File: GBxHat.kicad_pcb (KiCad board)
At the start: 2 copper layers, 65 x 30 mm, 30 parts, among them IC1 ATMEGA8515L-8AU, J0 Raspberry Pi, J1 AVR_SPI_6, U3 RT9013, U4 NLAS4157, U5 74LVC1G126SOT353-1, U6 74LVC1G126SOT353-1, X1 8MHz

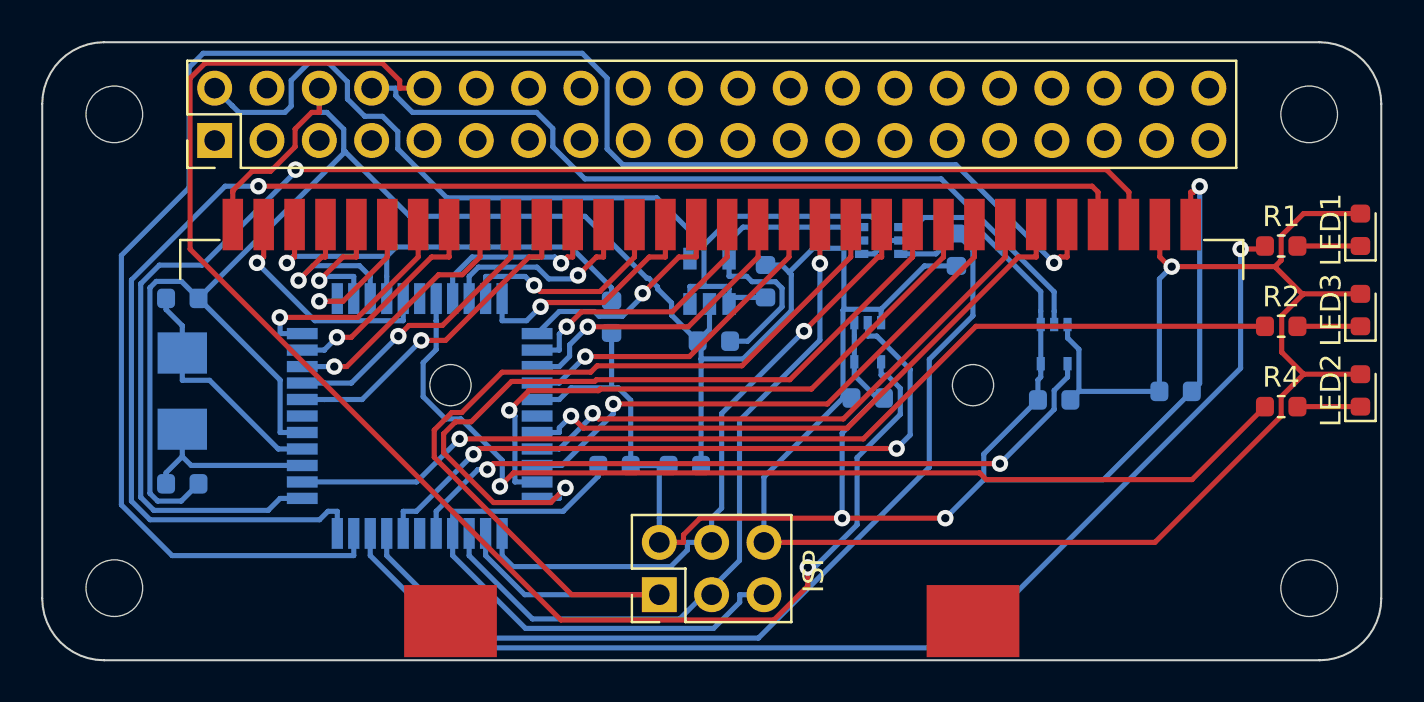
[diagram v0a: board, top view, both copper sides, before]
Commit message: Relocated & Updated LED's
Changed the identifiers for the LED's to match the GBxCart RW

Centered LED's on board
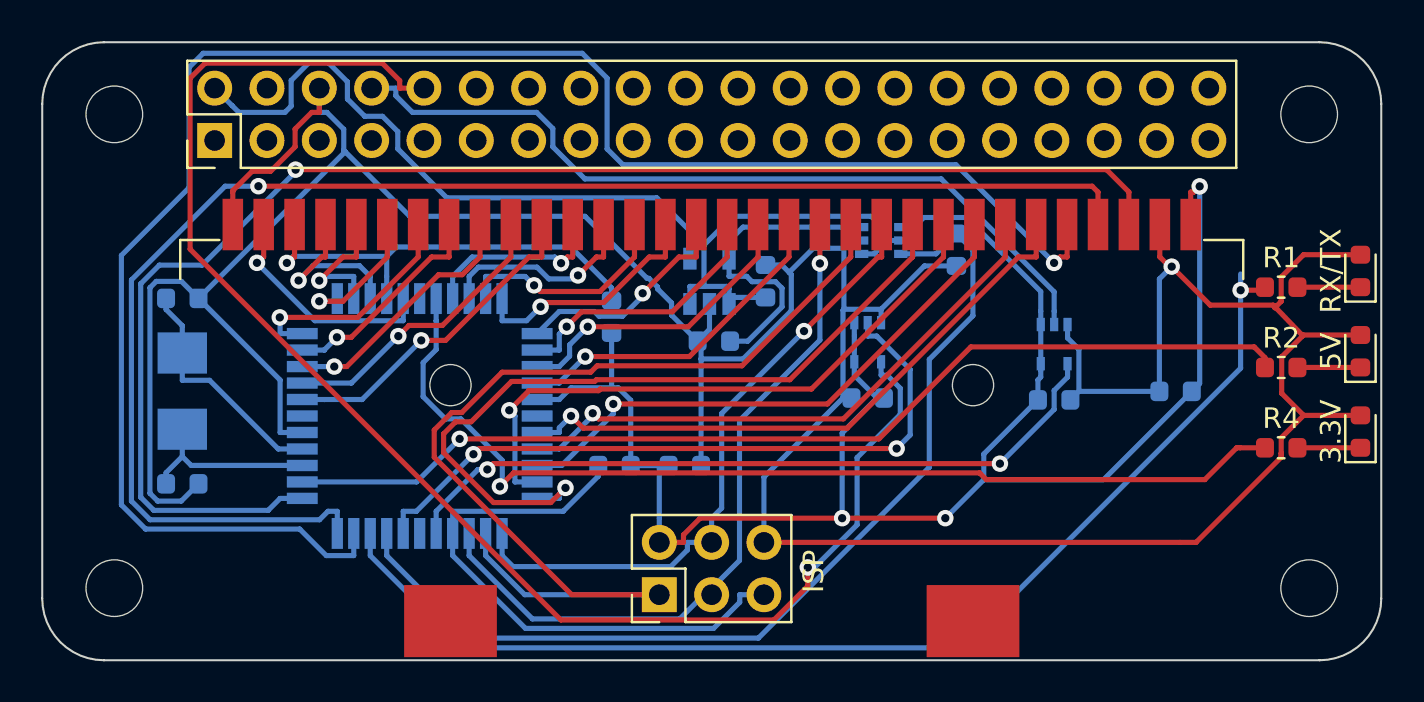
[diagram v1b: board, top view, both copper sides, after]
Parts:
- moved 3.3V 2.00 mm to (264.3, 86.2)
- moved 5V 2.00 mm to (264.3, 82.3)
- moved R1 2.00 mm to (260.4, 79.1)
- moved R2 2.00 mm to (260.4, 83.0)
- moved R4 2.00 mm to (260.4, 86.9)
- moved RX/TX 2.00 mm to (264.3, 78.4)
- renumbered LED2 to 3.3V, LED3 to 5V, LED1 to RX/TX
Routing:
- net Net-(IC1-Pad9): track 57.8 -> 56.6 mm
- net Net-(IC1-Pad29): track 50.5 -> 49.6 mm

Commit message: Fixed logic level issues & removed voltage regulator
- Fixed the issue where 5v logic was connected to the Pi zero which is not 5v tolerant
- Removed the NLAS4157, the 3.3v on the Pi zero itself is now being used instead
- Removed the 74LVC1G126 chips since RX and TX are now connected to the TXB0108
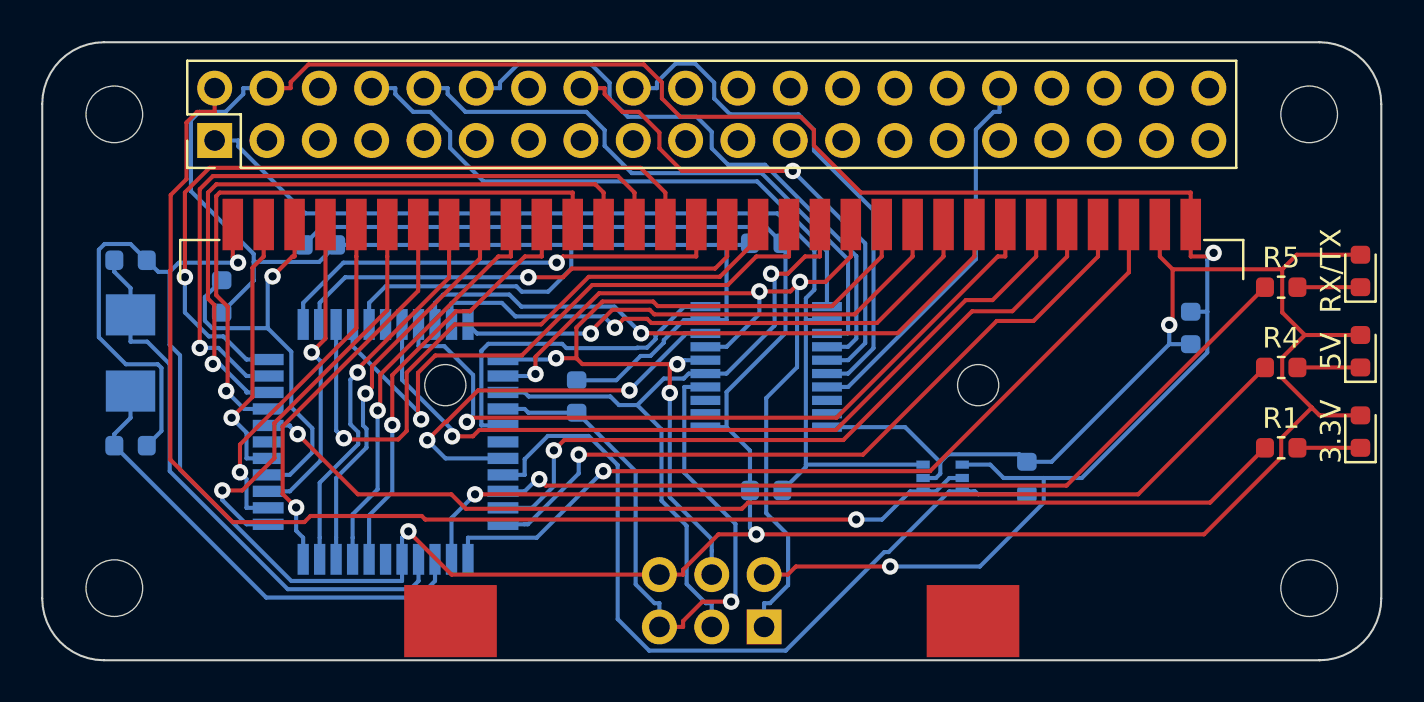
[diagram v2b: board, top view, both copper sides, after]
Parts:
- removed C10, C11, C8, C9: 0.1uF, Capacitor_SMD:C_0603_1608Metric
- removed C7: 1uF, Capacitor_SMD:C_0603_1608Metric
- removed the R5 at (228.0, 87.8)
- removed U3: RT9013, Package_TO_SOT_SMD:SOT-23-5
- removed U4: NLAS4157, Package_TO_SOT_SMD:SOT-363_SC-70-6
- removed U5, U6: 74LVC1G126SOT353-1, Package_TO_SOT_SMD:SOT-353_SC-70-5
- added C1: 0.1uF, Capacitor_SMD:C_0603_1608Metric, B.Cu at (235.4, 89.0)
- added C4: 0.1uF, Capacitor_SMD:C_0603_1608Metric, B.Cu at (213.7, 77.1)
- added C5: 0.1uF, Capacitor_SMD:C_0603_1608Metric, B.Cu at (235.4, 77.0)
- added R2: 10K, Resistor_SMD:R_0603_1608Metric, B.Cu at (226.2, 84.4)
- added U1: TXB0108PWR, Package_SO:TSSOP-20_4.4x6.5mm_P0.65mm, B.Cu at (235.4, 83.0)
- added U2: NLAS4157, Package_TO_SOT_SMD:SOT-363_SC-70-6, B.Cu at (244.0, 88.4)
- C6: value 1uF -> 0.1uF
- J0: value Raspberry Pi -> Pi Zero
- J1: moved to B.Cu
- moved C6 20.8 mm to (256.0, 81.1), turned to 270 degrees
- moved R6 19.0 mm to (209.0, 79.6)
- moved R3 11.6 mm to (248.1, 88.4), turned to 90 degrees
- moved J1 5.32 mm to (235.3, 95.6)
- moved C2 3.12 mm to (204.6, 86.8)
- moved C3 3.12 mm to (204.6, 77.8)
- moved X1 3.12 mm to (204.6, 82.3)
- moved IC1 2.08 mm to (216.9, 86.7), turned to 180 degrees
- renumbered C1 to C2, C2 to C3, R4 to R1, R2 to R4, R1 to R5
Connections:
- C6 pad 1: 5V -> VCC
- J0 pad 1: Net-(J0-Pad1) -> 3.3V
- J0 pad 10: /ATMEGA_TX_IN -> /PI_TX_IN
- J0 pad 12: Net-(J0-Pad12) -> /PI_MISO
- J0 pad 16: Net-(J0-Pad16) -> /PI_MOSI
- J0 pad 18: Net-(J0-Pad18) -> /PI_SCK
- J0 pad 21: (no net) -> Net-(J0-Pad21)
- J0 pad 22: (no net) -> Net-(J0-Pad22)
- J0 pad 23: (no net) -> Net-(J0-Pad23)
- J0 pad 24: (no net) -> Net-(J0-Pad24)
- J0 pad 25: (no net) -> Net-(J0-Pad25)
- J0 pad 26: (no net) -> Net-(J0-Pad26)
- J0 pad 27: (no net) -> Net-(J0-Pad27)
- J0 pad 28: (no net) -> Net-(J0-Pad28)
- J0 pad 29: (no net) -> Net-(J0-Pad29)
- J0 pad 30: (no net) -> Net-(J0-Pad30)
- J0 pad 31: (no net) -> Net-(J0-Pad31)
- J0 pad 32: (no net) -> /PI_RESET
- J0 pad 33: (no net) -> Net-(J0-Pad33)
- J0 pad 34: (no net) -> Net-(J0-Pad34)
- J0 pad 35: (no net) -> Net-(J0-Pad35)
- J0 pad 36: (no net) -> Net-(J0-Pad36)
- J0 pad 37: (no net) -> Net-(J0-Pad37)
- J0 pad 38: (no net) -> Net-(J0-Pad38)
- J0 pad 39: (no net) -> Net-(J0-Pad39)
- J0 pad 4: Net-(J0-Pad4) -> VCC
- J0 pad 40: (no net) -> Net-(J0-Pad40)
- J0 pad 6: GND -> Net-(J0-Pad6)
- J0 pad 8: /ATMEGA_RX_IN -> /PI_RX_IN
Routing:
- net /ATMEGA_TX_IN: track 72.3 -> 0.00 mm, vias 1 -> 0
- net VCC: track 87.5 -> 155.2 mm, vias 3 -> 2
- net /*MREQ/CS: track 86.8 -> 35.0 mm
- net /ATMEGA_RX_IN: track 39.5 -> 0.00 mm
- net /*RD: track 72.8 -> 36.4 mm
- net 3.3V: track 15.4 -> 50.5 mm
- net /*WR: track 71.1 -> 40.8 mm
- net /PI_MISO: track 0.00 -> 29.5 mm
- net /PI_TX_IN: track 0.00 -> 29.3 mm
- net /PI_RX_IN: track 0.00 -> 28.7 mm
- net /PI_SCK: track 0.00 -> 25.8 mm
- net /A12: track 11.9 -> 36.7 mm
- net /PI_MOSI: track 0.00 -> 24.6 mm, vias 0 -> 1
- net /A13: track 10.9 -> 34.8 mm
- net /A14: track 10.0 -> 32.9 mm
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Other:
- net class Default: trace_width 0.25 -> 0.2
- board text removed: "ISP"

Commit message: Fix an issue where VCC was bound to pin4 on the pi
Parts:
- MH1, MH2, MH3, MH4: value (none) -> MountingHole; footprint RPi_Hat:RPi_Hat_Mounting_Hole -> Custom:RPi_Hat_Mounting_Hole
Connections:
- J0 pad 4: VCC -> Net-(J0-Pad4)
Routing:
- net VCC: track 155.2 -> 159.4 mm, vias 2 -> 3

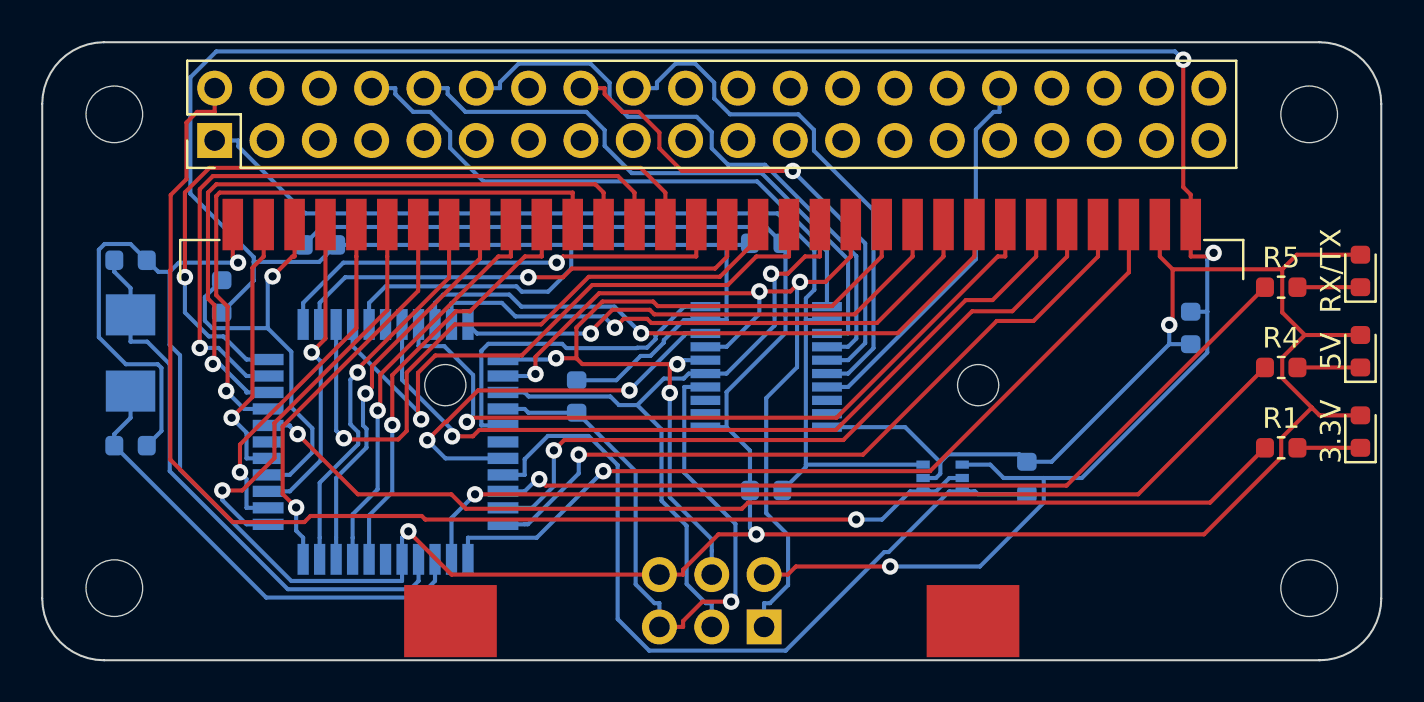
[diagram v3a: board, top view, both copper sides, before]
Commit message: Moved the LED resistors to the other side of the board as they were in the way of the cart slot
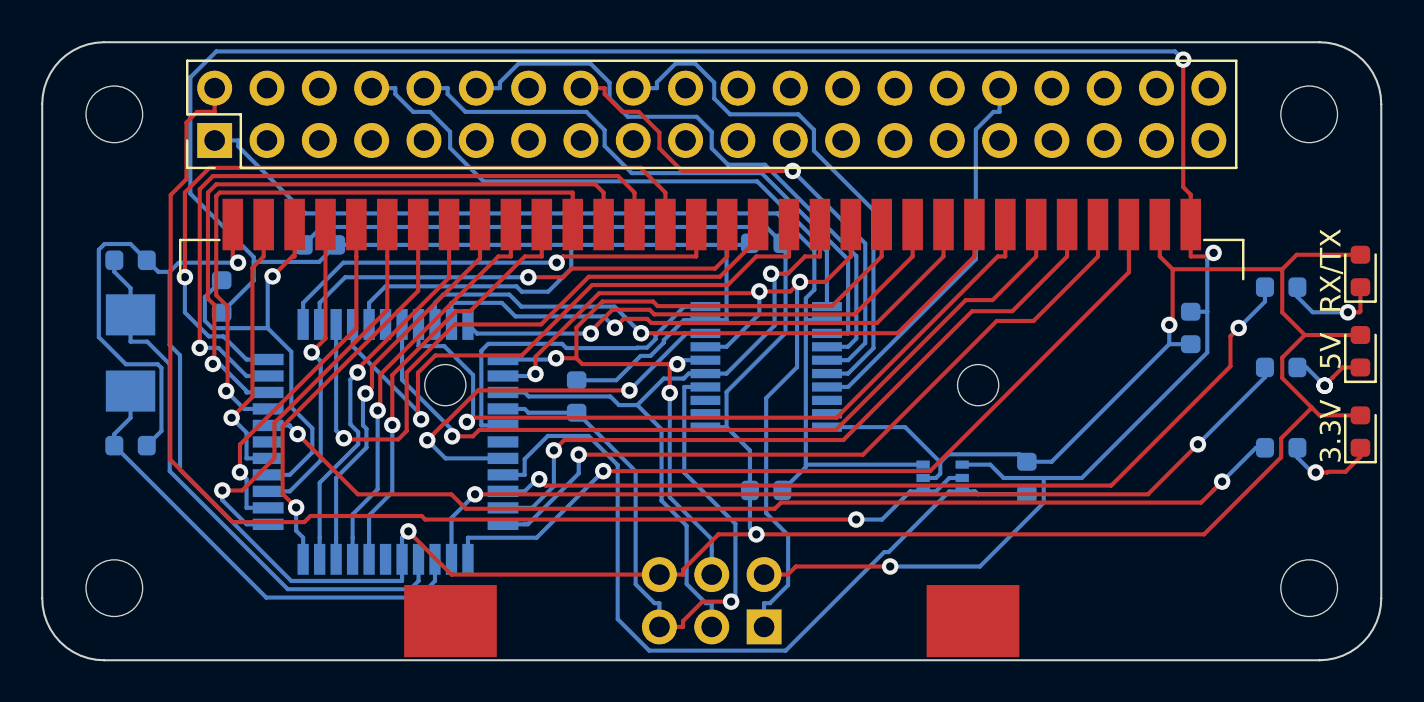
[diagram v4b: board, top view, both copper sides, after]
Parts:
- R1, R4, R5: moved to B.Cu
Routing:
- net Net-(LED3-Pad1): track 3.06 -> 5.04 mm, vias 0 -> 1
- net Net-(LED1-Pad1): track 3.06 -> 4.58 mm, vias 0 -> 1
- net Net-(IC1-Pad9): track 41.3 -> 42.6 mm, vias 1 -> 2
- net Net-(LED2-Pad1): track 3.06 -> 3.80 mm, vias 0 -> 2
- net Net-(IC1-Pad13): track 44.5 -> 44.8 mm, vias 1 -> 2
- net Net-(IC1-Pad29): vias 1 -> 2

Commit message: small update
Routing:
- net Net-(LED2-Pad1): vias 2 -> 1
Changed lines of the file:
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@@
     (thickness 1.6)
     (drawings 10)
-    (tracks 729)
+    (tracks 728)
     (zones 0)
     (modules 26)
@@
   (segment (start 261.1935 83.0382) (end 261.631 83.0382) (width 0.2) (layer B.Cu) (net 58))
   (segment (start 262.51043 83.91763) (end 262.52202 83.92922) (width 0.2) (layer B.Cu) (net 58))
-  (via (at 262.51043 83.91763) (size 0.8) (drill 0.4) (layers F.Cu B.Cu) (net 58))
   (segment (start 262.52202 83.92922) (end 262.52202 83.92922) (width 0.2) (layer B.Cu) (net 58))
-  (via (at 262.52202 83.92922) (size 0.8) (drill 0.4) (layers F.Cu B.Cu) (net 58))
   (segment (start 262.910429 83.517631) (end 262.51043 83.91763) (width 0.2) (layer F.Cu) (net 58))
   (segment (start 263.38986 83.0382) (end 262.910429 83.517631) (width 0.2) (layer F.Cu) (net 58))
   (segment (start 264.252 83.0382) (end 263.38986 83.0382) (width 0.2) (layer F.Cu) (net 58))
+  (via (at 262.51043 83.91763) (size 0.8) (drill 0.4) (layers F.Cu B.Cu) (net 58) (status 1000000))
   (segment (start 261.1935 79.6157) (end 261.93832 80.36052) (width 0.2) (layer B.Cu) (net 59))
   (segment (start 261.1935 79.1407) (end 261.1935 79.6157) (width 0.2) (layer B.Cu) (net 59))
